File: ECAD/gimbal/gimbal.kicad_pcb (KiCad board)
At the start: 2 copper layers, 47.6 x 39.4 mm, 15 parts, among them J1 PWR, J2 UPDI, J3 BNO1, J4 Servo, J5 UART, J6 NOTIF, J7 Servo, J8 BNO2, J9 Servo, U1 LM1117-3.3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

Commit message: v2 for A5100 gimbal
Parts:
- removed the J6 at (128.9, 87.0)
- removed J9: Servo, Connector_PinHeader_2.54mm:PinHeader_1x03_P2.54mm_Vertical
- added H1: MountingHole, MountingHole:MountingHole_3.2mm_M3, F.Cu at (152.1, 122.2)
- added SW1: POWER, gimbal:Switch, F.Cu at (139.2, 121.8)
- D1: value MBR0520LT1G -> BAT54
- J1: footprint Connector_PinHeader_2.54mm:PinHeader_1x02_P2.54mm_Vertical -> Connector_PinHeader_2.54mm:PinHeader_1x03_P2.54mm_Vertical
- moved J6 44.9 mm to (173.6, 121.9), turned to -90 degrees
- moved J1 44.3 mm to (122.6, 121.9), turned to 90 degrees
- moved J4 44.1 mm to (163.7, 121.9), turned to -90 degrees
- moved C1 37.0 mm to (131.7, 117.0), turned to 180 degrees
- moved D1 36.1 mm to (137.5, 113.9), turned to 90 degrees
- moved U1 31.6 mm to (131.8, 110.5), turned to 90 degrees
- moved C2 22.2 mm to (137.5, 108.6), turned to -90 degrees
- moved J2 20.1 mm to (131.2, 102.1)
- moved J5 13.5 mm to (142.4, 95.0), turned to 180 degrees
- moved U2 12.9 mm to (145.7, 105.9), turned to 180 degrees
- moved R1 10.2 mm to (137.8, 102.7), turned to 0 degrees
- moved J3 8.60 mm to (154.3, 85.0)
- moved J7 8.60 mm to (172.1, 87.5)
- renumbered J7 to J6, J8 to J7
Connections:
- J1 pad 1: VCC -> GND
- J1 pad 2: GND -> Net-(J1-Pad2)
- J3 pad 2: (no net) -> unconnected-(J3-Pad2)
- J3 pad 6: (no net) -> unconnected-(J3-Pad6)
- J7 pad 1: (no net) -> unconnected-(J7-Pad1)
- J7 pad 2: (no net) -> unconnected-(J7-Pad2)
- J7 pad 3: (no net) -> unconnected-(J7-Pad3)
- J7 pad 4: (no net) -> unconnected-(J7-Pad4)
- U2 pad 11: (no net) -> unconnected-(U2-Pad11)
- U2 pad 12: (no net) -> unconnected-(U2-Pad12)
- U2 pad 13: /Servo_Z -> unconnected-(U2-Pad13)
- U2 pad 4: /NOTIF -> unconnected-(U2-Pad4)
- U2 pad 5: (no net) -> unconnected-(U2-Pad5)
- U2 pad 6: (no net) -> unconnected-(U2-Pad6)
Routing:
- net /Servo_Z: track 34.1 -> 0.00 mm, vias 1 -> 0
- net +3V3: track 49.0 -> 76.2 mm, vias 0 -> 2
- net Net-(J1-Pad2): track 0.00 -> 16.6 mm
- net /Servo_Y: track 43.5 -> 31.6 mm, vias 1 -> 0
- net /NOTIF: track 11.7 -> 0.00 mm
- net /Servo_X: track 37.6 -> 26.0 mm, vias 1 -> 0
- net VCC: track 42.4 -> 54.0 mm
- net GND: track 0.00 -> 3.83 mm
- net /SDA: track 12.3 -> 15.1 mm, vias 1 -> 0
- net Net-(R1-Pad2): track 3.95 -> 4.73 mm
- net /UPDI: track 4.67 -> 5.41 mm
- net /SCL: track 13.9 -> 14.5 mm
- net /TX: track 8.89 -> 9.50 mm, vias 0 -> 1
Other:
- board size 47.6 x 39.4 mm -> 61 x 74 mm
- net class Default removed
- board text added: "5-7.2V INPUT X Servo - 0 Y Servo - 1 UART 3.3V Logic, TX Only"
- board text added: "Gimbal Servo Control Alan H. v2"
- board text added: "POWER IN"
- board text added: "TJHSST UAV"
- board text added: "UART"
- board text added: "X SERVO"
- board text added: "Y SERVO"
- board text removed: "Gimbal Servo Control Alan H. v1"
- board text removed: "NOTIF"
- board text removed: "VIN"
- board text removed: "X"
- board text removed: "Y"
- board text removed: "Z"

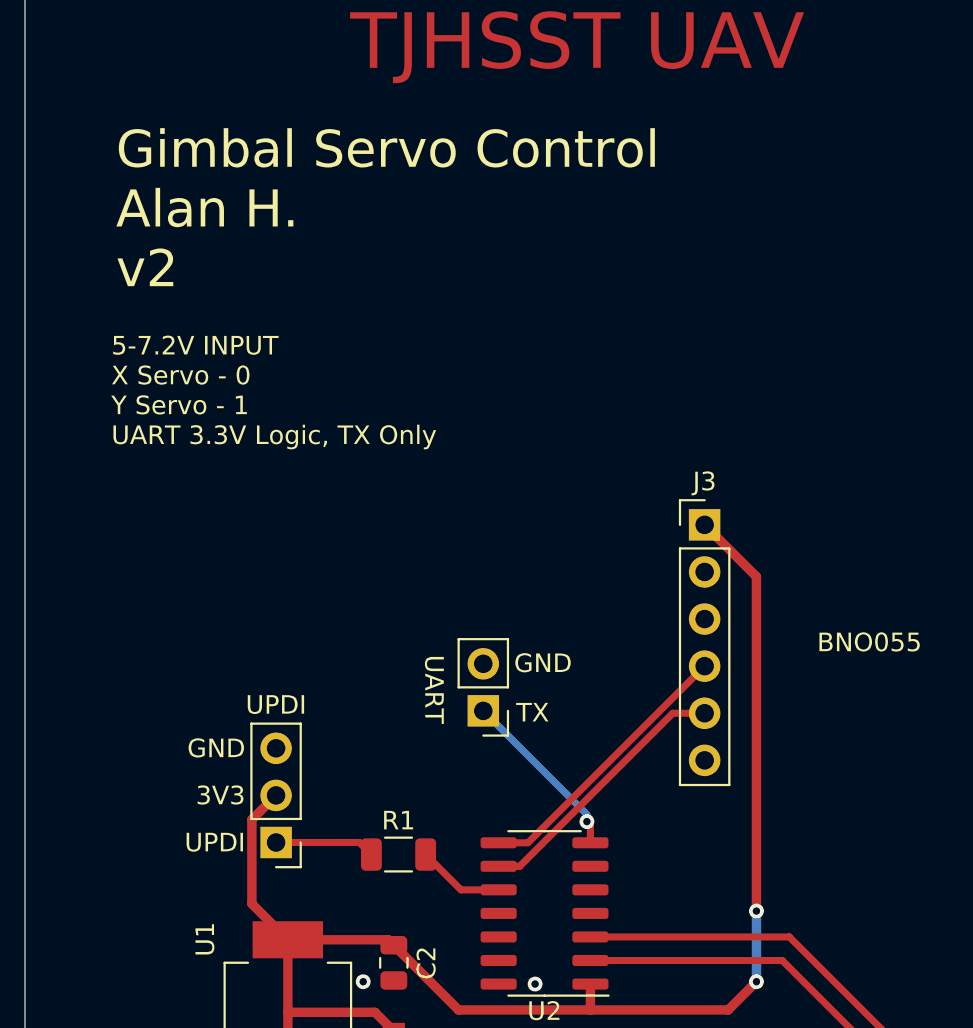
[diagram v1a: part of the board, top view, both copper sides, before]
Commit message: Add centering and remove buttons
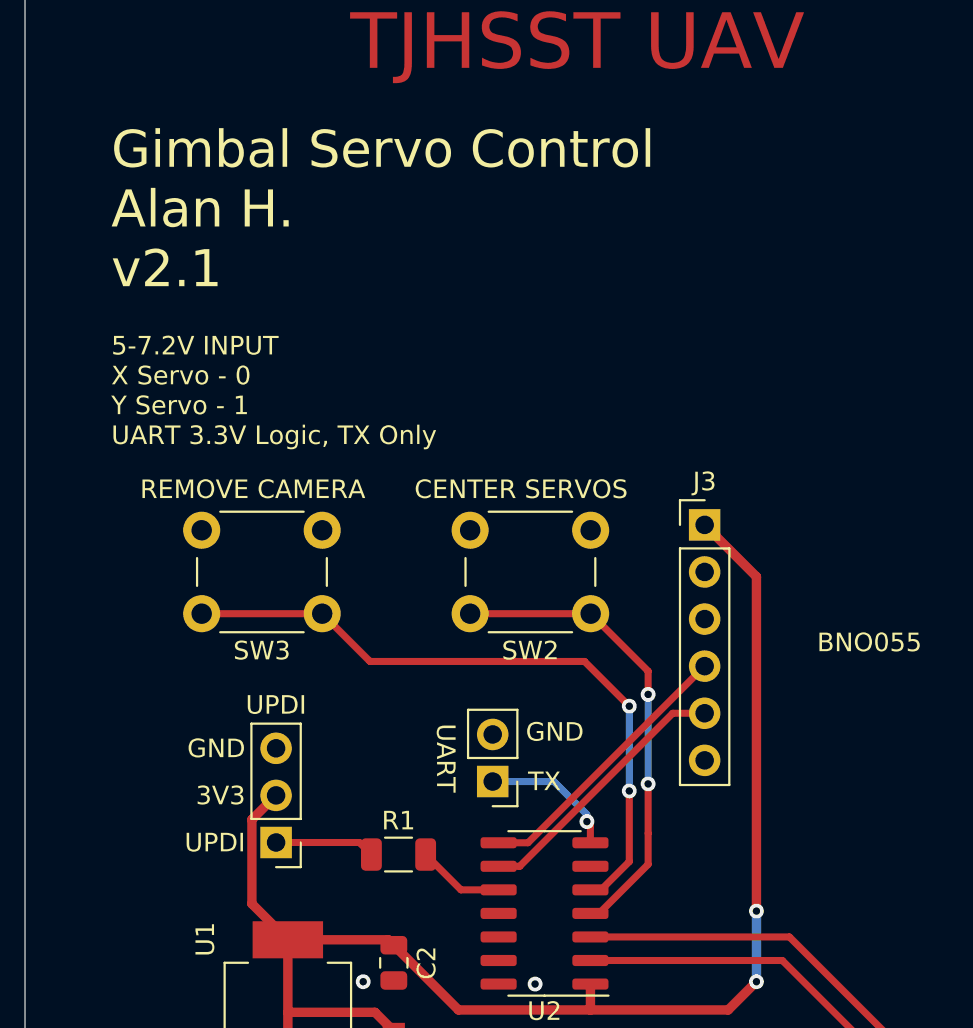
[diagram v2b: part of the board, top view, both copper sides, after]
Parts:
- added SW2: CENTER SERVOS, Button_Switch_THT:SW_PUSH_6mm, F.Cu at (148.2, 89.8)
- added SW3: REMOVE CAMERA, Button_Switch_THT:SW_PUSH_6mm, F.Cu at (133.7, 89.8)
- moved J5 3.84 mm to (142.9, 98.8)
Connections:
- U2 pad 4: unconnected-(U2-Pad4) -> /Center
- U2 pad 5: unconnected-(U2-Pad5) -> /Side
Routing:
- net /Side: track 0.00 -> 36.2 mm, vias 0 -> 2
- net /Center: track 0.00 -> 25.5 mm, vias 0 -> 2
- net /TX: track 9.50 -> 7.42 mm
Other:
- board text added: "Gimbal Servo Control Alan H. v2.1"
- board text removed: "Gimbal Servo Control Alan H. v2"

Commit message: update footprints
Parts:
- removed J5: UART, Connector_PinHeader_2.54mm:PinHeader_1x02_P2.54mm_Vertical
- added D2: POWER, Diode_SMD:D_0805_2012Metric, F.Cu at (198.1, 106.7)
- added D3: CENTERED, Diode_SMD:D_0805_2012Metric, F.Cu at (197.4, 109.8)
- added D4: REMOVED, Diode_SMD:D_0805_2012Metric, F.Cu at (202.6, 106.7)
- added R2: 1K, Resistor_SMD:R_1206_3216Metric, F.Cu at (192.3, 110.0)
- added R3: 1K, Resistor_SMD:R_1206_3216Metric, F.Cu at (186.7, 110.0)
- added R4: 1K, Resistor_SMD:R_1206_3216Metric, F.Cu at (198.7, 103.5)
- added SW4: PRGM/DEBUG, Button_Switch_THT:SW_Slide_1P2T_CK_OS102011MS2Q, F.Cu at (187.9, 105.4)
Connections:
- J2 pad 1: /UPDI -> Net-(J2-Pad1)
- U2 pad 12: unconnected-(U2-Pad12) -> Net-(R4-Pad1)
- U2 pad 13: unconnected-(U2-Pad13) -> Net-(R3-Pad1)
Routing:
- net Net-(J2-Pad1): track 0.00 -> 5.41 mm
- net /UPDI: track 5.41 -> 0.00 mm

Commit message: v2.2 complete
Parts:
- J2: value UPDI -> UPDI/DEBUG
- moved D4 78.8 mm to (130.6, 74.8)
- moved D2 75.0 mm to (123.4, 113.8), turned to 90 degrees
- moved R4 73.0 mm to (130.6, 77.2)
- moved R2 66.5 mm to (126.0, 113.8), turned to 90 degrees
- moved D3 63.3 mm to (144.7, 74.7), turned to 180 degrees
- moved R3 53.3 mm to (144.7, 77.2), turned to 180 degrees
- moved SW4 49.3 mm to (139.7, 95.0)
- moved SW2 3.39 mm to (148.2, 86.4)
- moved SW3 3.39 mm to (133.7, 86.4)
- moved R1 0.40 mm to (137.7, 103.1), turned to -90 degrees
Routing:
- net Net-(R4-Pad1): track 0.00 -> 46.6 mm, vias 0 -> 2
- net Net-(R3-Pad1): track 0.00 -> 37.9 mm, vias 0 -> 2
- net Net-(J2-Pad1): track 5.41 -> 17.0 mm
- net VCC: track 54.0 -> 64.9 mm
- net /UPDI: track 0.00 -> 7.51 mm
- net /Center: track 25.5 -> 28.9 mm
- net Net-(D3-Pad2): track 0.00 -> 2.76 mm
- net Net-(D2-Pad2): track 0.00 -> 2.76 mm
- net Net-(D4-Pad2): track 0.00 -> 2.66 mm
- net /TX: track 7.42 -> 9.80 mm
- net /Side: track 36.2 -> 37.6 mm
- net Net-(R1-Pad2): track 4.73 -> 5.55 mm
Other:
- board text added: "Gimbal Servo Control Alan H. v2.2"
- board text added: "UART/UPDI"
- board text removed: "Gimbal Servo Control Alan H. v2.1"
- board text removed: "TX"
- board text removed: "UART"
- board text removed: "UPDI"
